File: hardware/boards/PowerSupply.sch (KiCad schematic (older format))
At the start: 6 parts

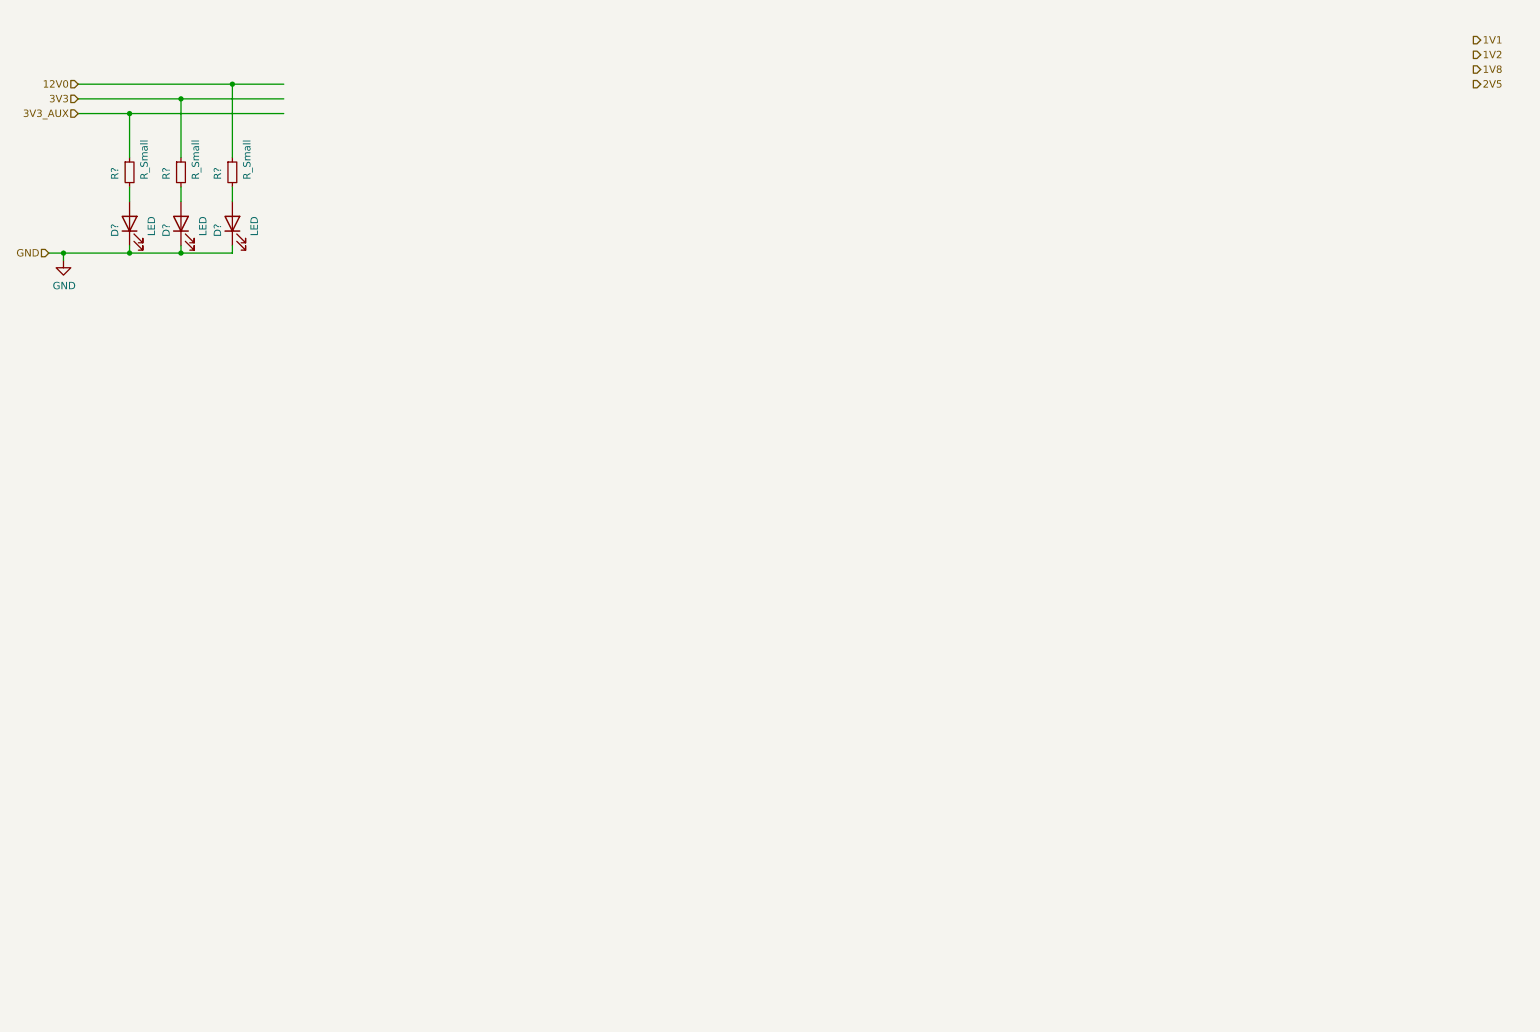
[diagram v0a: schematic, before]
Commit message: A bit of work on the power supply, the values still need to be calculated, but all the passives and such should be there
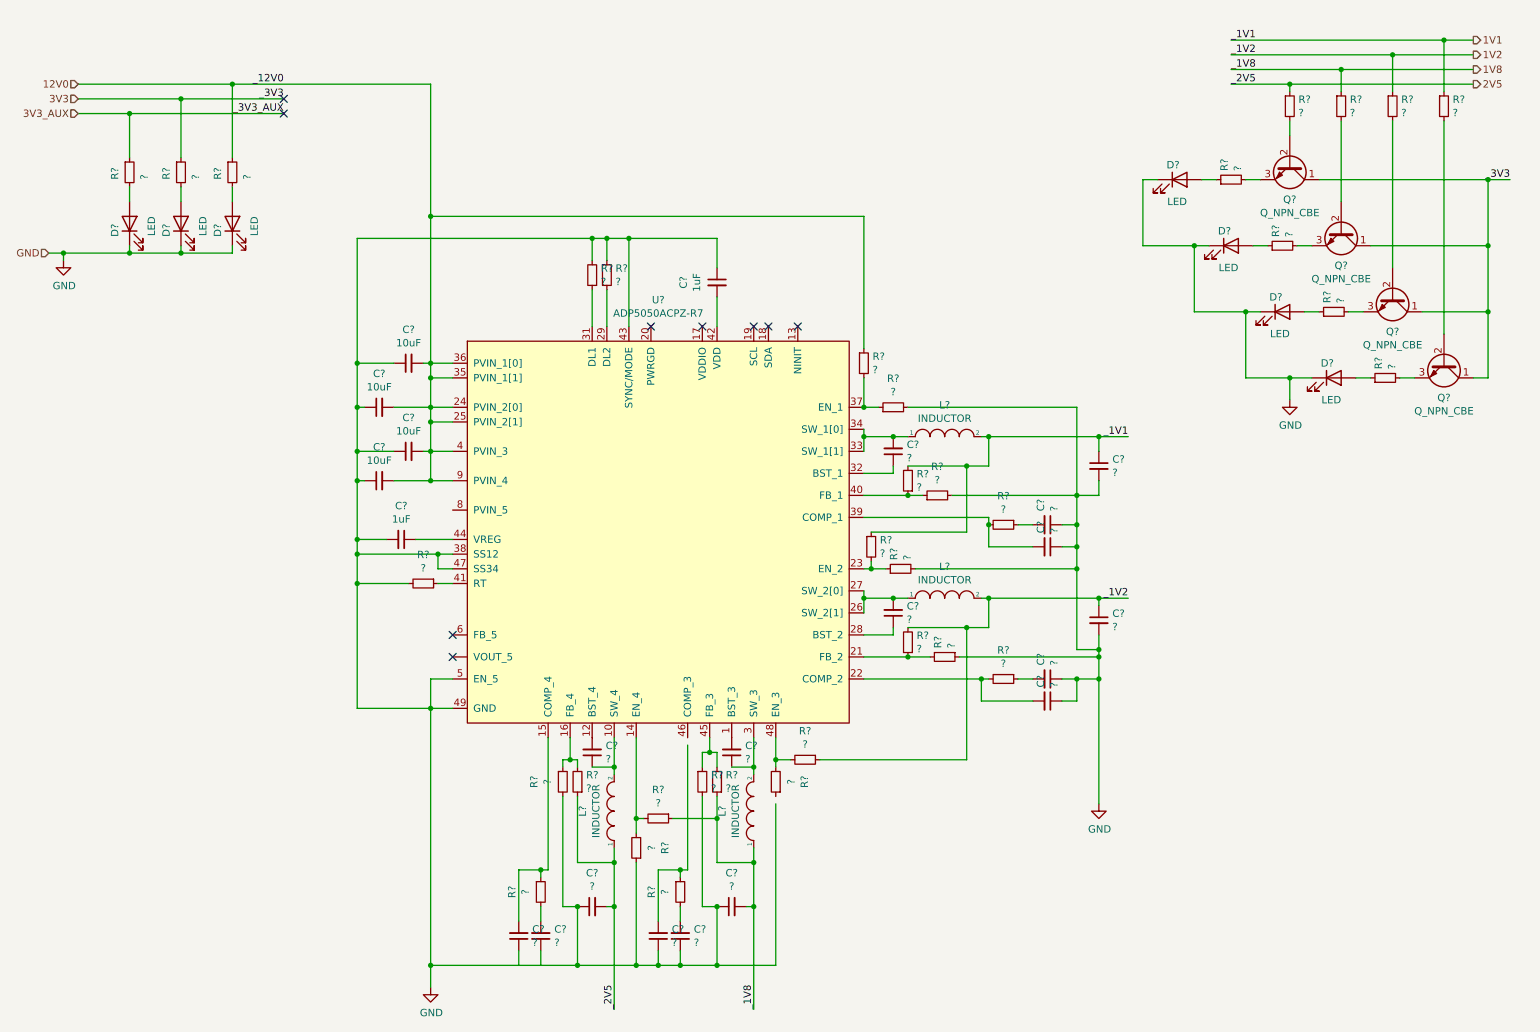
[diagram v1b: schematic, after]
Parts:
- added C? (x2): 1uF, Capacitor_SMD:C_0603_1608Metric, symbol Device:C_Small
- added C? (x4): ?, Capacitor_SMD:C_1206_3216Metric, symbol Device:C_Small
- added C? (x4): 10uF, Capacitor_SMD:C_1206_3216Metric, symbol Device:C_Small
- added C? (x12): ?, Capacitor_SMD:C_0603_1608Metric, symbol Device:C_Small
- added D? (x4): LED, symbol Device:LED
- added L? (x4): INDUCTOR, symbol pspice:INDUCTOR
- added Q? (x4): Q_NPN_CBE, symbol Device:Q_NPN_CBE
- added R? (x31): ?, symbol Device:R_Small
- added U?: ADP5050ACPZ-R7, lethalbit:QFN-48_EP_7x7_Pitch0.5mm, symbol lethalbit:ADP5050ACPZ-R7
- R? (x3): value R_Small -> ?
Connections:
- net labels added: _12V0, _1V1, _1V2, _1V8, _2V5, _3V3, _3V3_AUX
- wire segments 20 -> 256
- no-connect marks 0 -> 9

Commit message: Updated part mfr and added the proper part numbers
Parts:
- U?: MFR (none) -> Analog Devices; MPN (none) -> ADP5050ACPZ-R7
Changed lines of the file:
@@
 F 2 "lethalbit:QFN-48_EP_7x7_Pitch0.5mm" H 5250 4150 50  0001 C CNN
 F 3 "https://www.analog.com/media/en/technical-documentation/data-sheets/ADP5050.PDF" H 5250 4150 50  0001 C CNN
+F 4 "Analog Devices" H 5250 4100 50  0001 C CNN "MFR"
+F 5 " ADP5050ACPZ-R7 " H 5250 4100 50  0001 C CNN "MPN"
 	1    5250 4100
 	1    0    0    -1

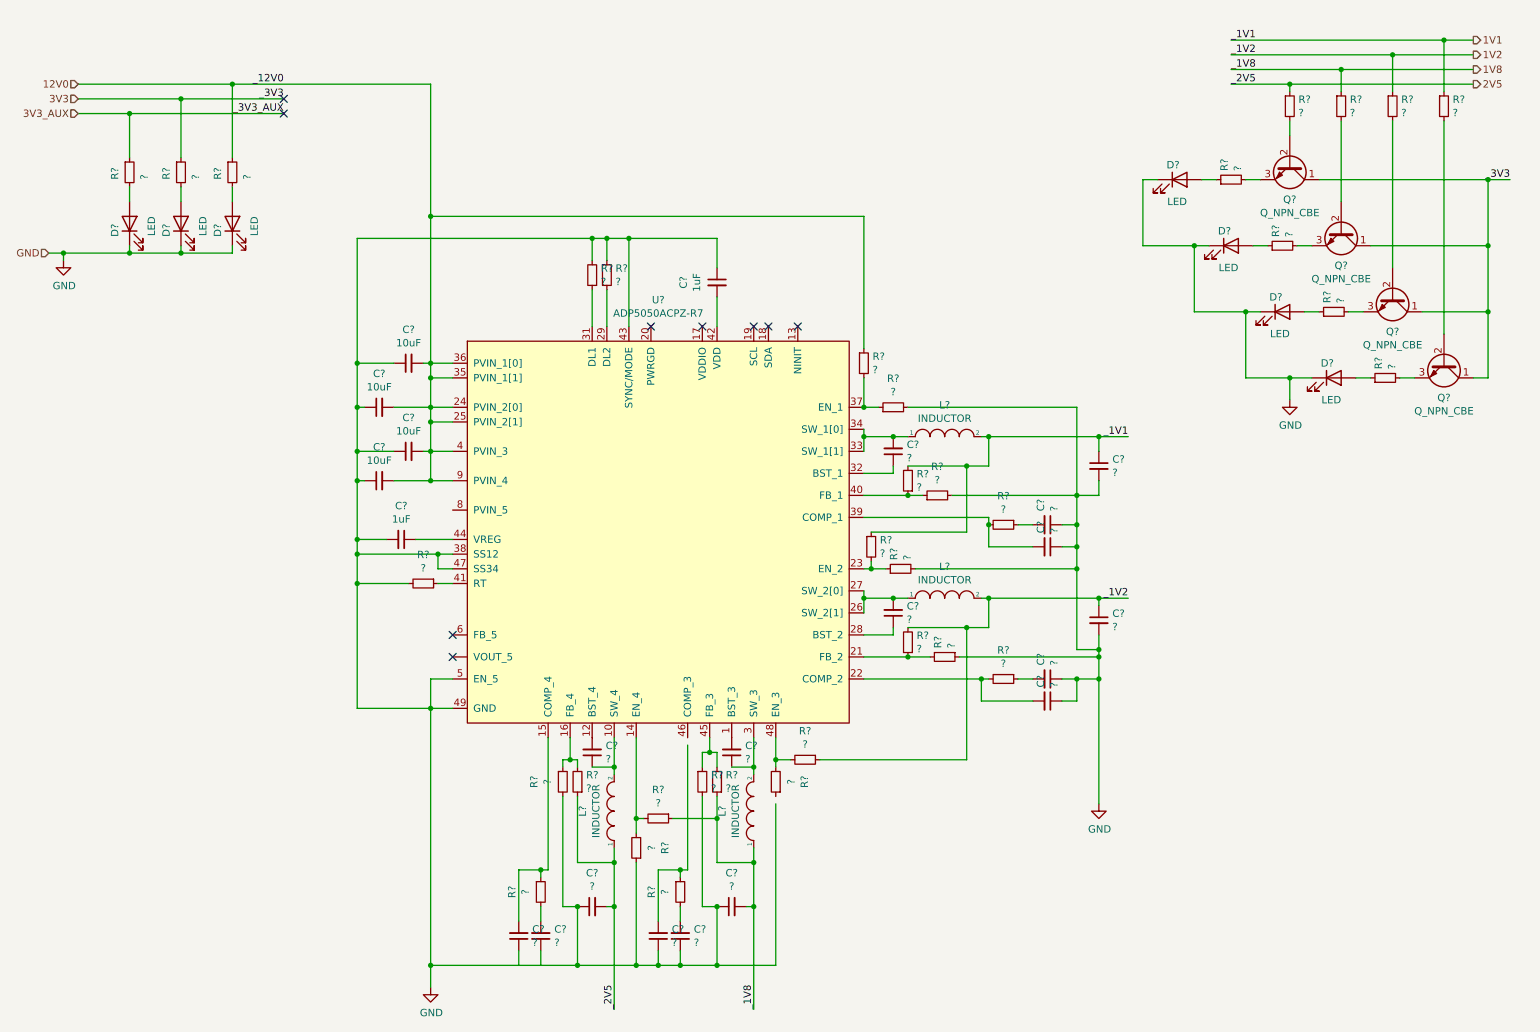
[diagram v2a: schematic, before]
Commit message: Did some annotation and fixed the FPGA bank that was accidentally labled as the cypress part
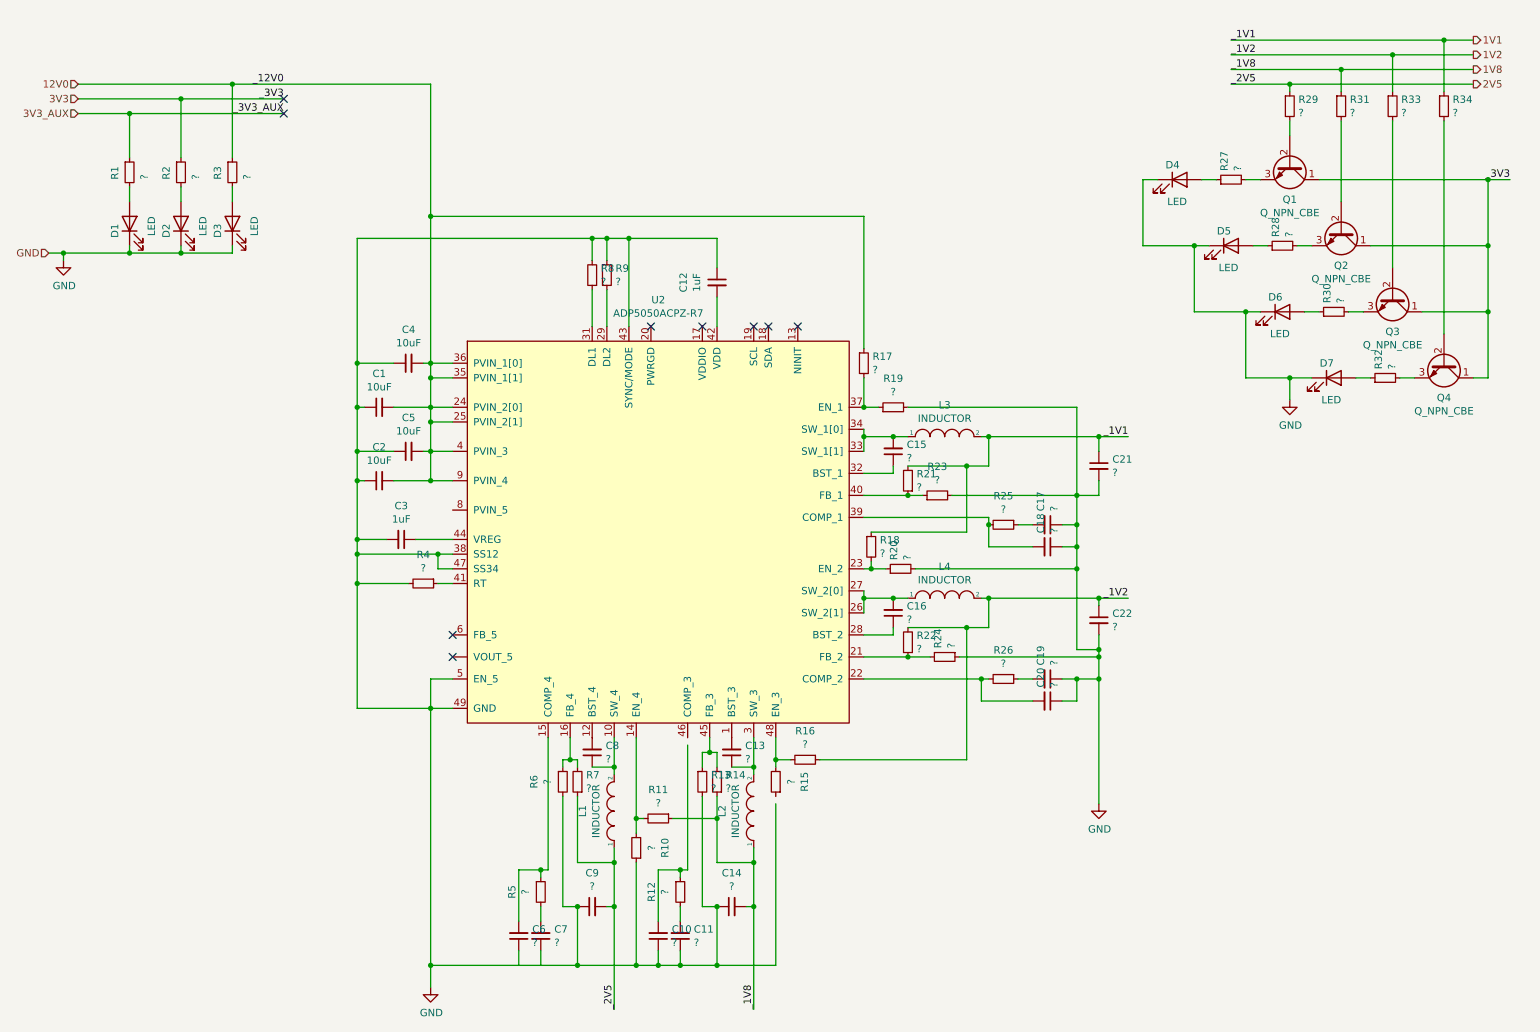
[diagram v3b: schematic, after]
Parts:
- gave numbers to parts that had none: 72

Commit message: Lots of small updates, getting values specified for parts, switched the BJT to NFETs
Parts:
- removed Q1, Q2, Q3, Q4: Q_NPN_CBE, symbol Device:Q_NPN_CBE
- added Q1, Q2, Q3, Q4: Q_NMOS_GSD, Package_TO_SOT_SMD:SOT-23, symbol Device:Q_NMOS_GSD
- D1, D2, D3, D4, D5, D6, D7: value LED -> GRN; footprint (none) -> LED_SMD:LED_0603_1608Metric; MFR (none) -> Würth Elektronik; MPN (none) -> 150060GS75000
- R1, R2, R31, R32, R33, R34: value ? -> 20; footprint (none) -> Resistor_SMD:R_0603_1608Metric; MFR (none) -> Vishay Dale; MPN (none) -> CRCW060320R0JNEA
- R27, R28, R29, R30: value ? -> 10k; footprint (none) -> Resistor_SMD:R_0603_1608Metric; MFR (none) -> Vishay Dale; MPN (none) -> CRCW060310K0FKEA
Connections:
- net 1V2: now also R28.1; no longer R33.1
- net 1V8: now also R27.1; no longer R31.1
- net 3V3: now also R31.1, R32.1, R33.1, R34.1
- net GND: now also Q1.2 (S), Q2.2 (S), Q3.2 (S), Q4.2 (S); no longer D4.1 (K), D5.1 (K), D6.1 (K), D7.1 (K)
- net at R29.2: now also Q1.1 (G)
- net at R27.2: now also Q2.1 (G)
- net at R33.2: now also D7.2 (A)
- net at R30.2: now also Q4.1 (G)
- net at R31.2: now also D5.2 (A)
- net at R28.2: now also Q3.1 (G)
- net at R34.2: now also D4.2 (A)
- net at R32.2: now also D6.2 (A)
- net 1V5: now reaches R30.1
- net 1V5: now also C21.1, L3.2, R18.1, R21.2; no longer D6.2 (A)
- removed net 1V1: C21.1, L3.2, R18.1, R21.2, R34.1
- new net: D7.1 (K), Q3.3 (D)
- new net: D6.1 (K), Q2.3 (D)
- new net: D5.1 (K), Q1.3 (D)
- new net: D4.1 (K), Q4.3 (D)
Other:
- moved on the sheet: D4, R29
